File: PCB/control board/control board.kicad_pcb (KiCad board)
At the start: 2 copper layers, 27 parts, among them J1 JST-XH 1x05, J2 JST-XH 1x05, J3 JST-XH 1x05, SW1 SW_MEC_5E, SW2 SW_MEC_5E, SW3 SW_MEC_5E, SW4 SW_MEC_5E, SW5 SW_MEC_5E, SW6 SW_MEC_5E, SW7 SW_MEC_5E, SW8 SW_MEC_5E

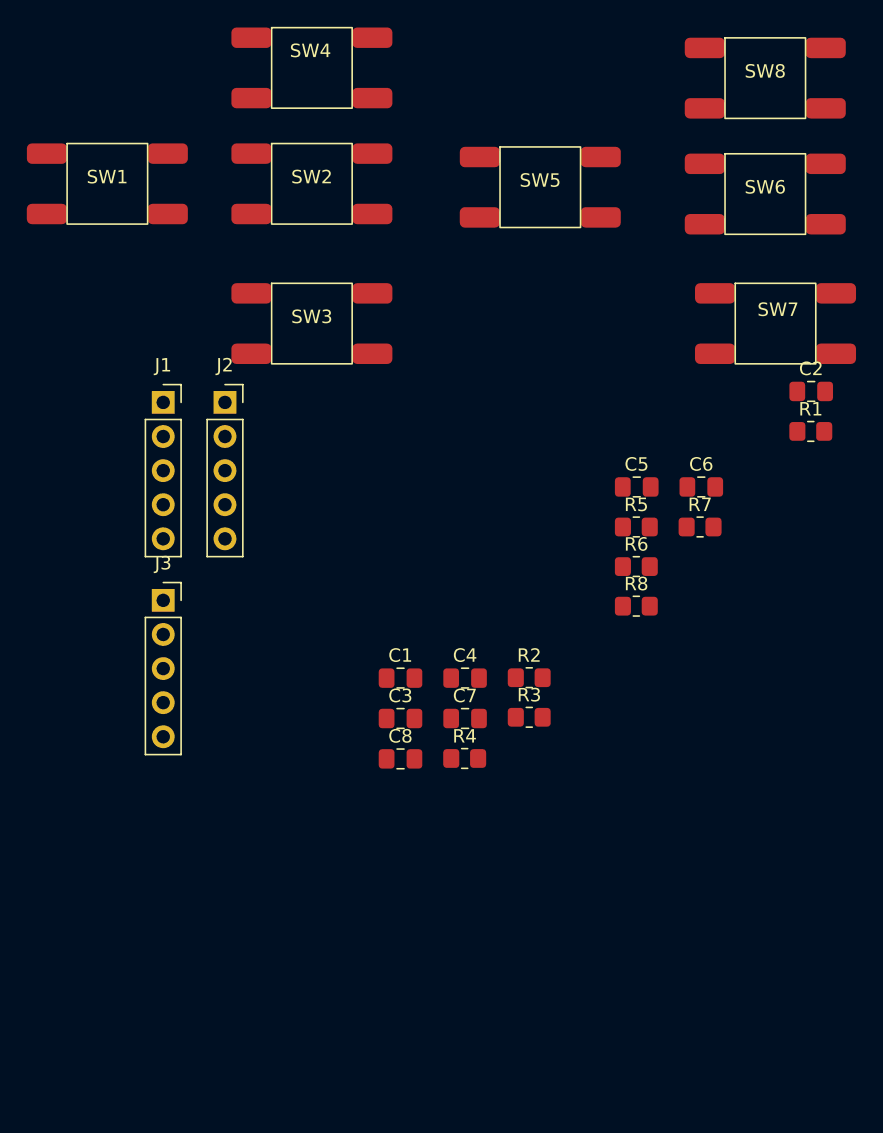
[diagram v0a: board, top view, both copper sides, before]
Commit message: Led board + control board
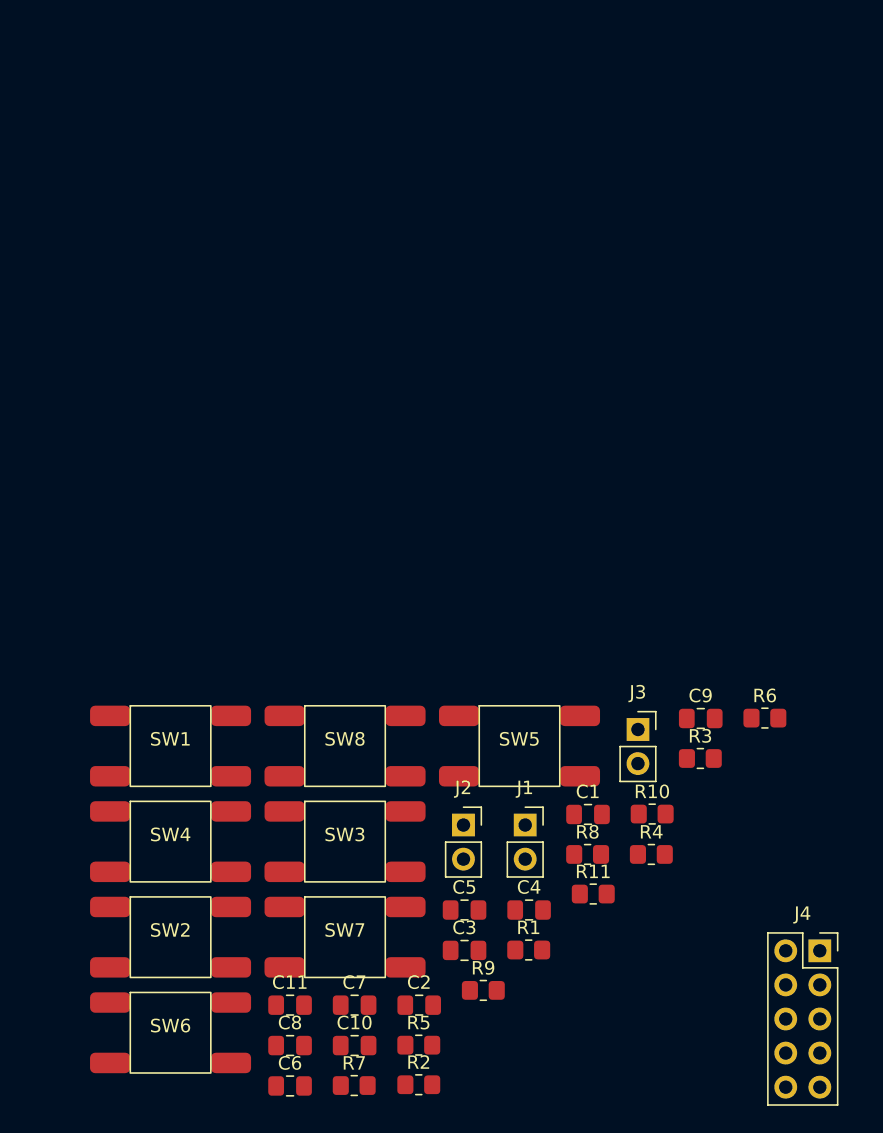
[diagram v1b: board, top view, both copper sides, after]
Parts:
- added C10: 100nF, Capacitor_SMD:C_0805_2012Metric_Pad1.18x1.45mm_HandSolder, F.Cu at (127.4, 125.9)
- added C11: 100nF, Capacitor_SMD:C_0805_2012Metric_Pad1.18x1.45mm_HandSolder, F.Cu at (122.6, 122.9)
- added C9: 100nF, Capacitor_SMD:C_0805_2012Metric_Pad1.18x1.45mm_HandSolder, F.Cu at (153.2, 101.6)
- added J4: Conn_02x05_Top_Bottom, Connector_PinSocket_2.54mm:PinSocket_2x05_P2.54mm_Vertical, F.Cu at (162.1, 118.9)
- added R10: 10k, Resistor_SMD:R_0805_2012Metric_Pad1.20x1.40mm_HandSolder, F.Cu at (149.6, 108.7)
- added R11: 10k, Resistor_SMD:R_0805_2012Metric_Pad1.20x1.40mm_HandSolder, F.Cu at (145.2, 114.6)
- added R9: 10k, Resistor_SMD:R_0805_2012Metric_Pad1.20x1.40mm_HandSolder, F.Cu at (137.0, 121.8)
- J1: value JST-XH 1x05 -> BTN1; footprint Connector_PinSocket_2.54mm:PinSocket_1x05_P2.54mm_Vertical -> Connector_PinSocket_2.54mm:PinSocket_1x02_P2.54mm_Vertical
- J2: value JST-XH 1x05 -> BTN2; footprint Connector_PinSocket_2.54mm:PinSocket_1x05_P2.54mm_Vertical -> Connector_PinSocket_2.54mm:PinSocket_1x02_P2.54mm_Vertical
- J3: value JST-XH 1x05 -> BTN3; footprint Connector_PinSocket_2.54mm:PinSocket_1x05_P2.54mm_Vertical -> Connector_PinSocket_2.54mm:PinSocket_1x02_P2.54mm_Vertical
- moved SW6 76.6 mm to (113.7, 125.0)
- moved SW8 58.8 mm to (126.7, 103.6)
- moved SW4 58.6 mm to (113.7, 110.7)
- moved SW2 57.1 mm to (113.7, 117.9)
- moved SW7 55.8 mm to (126.7, 117.9)
- moved C2 54.3 mm to (132.2, 122.9)
- moved C6 54.1 mm to (122.6, 128.9)
- moved R7 49.0 mm to (127.4, 128.9)
- moved R1 44.0 mm to (140.4, 118.8)
- moved SW1 42.2 mm to (113.7, 103.6)
- moved R5 41.9 mm to (132.2, 125.9)
- moved SW5 41.7 mm to (139.7, 103.6)
- moved J1 41.5 mm to (140.1, 109.5)
- moved SW3 38.7 mm to (126.7, 110.7)
- moved J3 36.7 mm to (148.5, 102.4)
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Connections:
- C2 pad 1: OK -> MENU
- C3 pad 1: DOWN -> OK
- C4 pad 1: UP -> DOWN
- C5 pad 1: RIGHT -> HOME
- C6 pad 1: BTN2 -> UP
- C7 pad 1: BTN3 -> RIGHT
- C8 pad 1: BTN1 -> BACK
- J1 pad 1: +3.3V -> GND
- J1 pad 2: UP -> BTN1
- J2 pad 1: OK -> GND
- J2 pad 2: BTN1 -> BTN2
- J3 pad 1: unconnected-(J3-Pad1) -> GND
- J3 pad 2: unconnected-(J3-Pad2) -> BTN3
- SW2 pad 3: OK -> MENU
- SW3 pad 3: DOWN -> OK
- SW4 pad 3: UP -> DOWN
- SW5 pad 3: RIGHT -> HOME
- SW6 pad 3: BTN2 -> UP
- SW7 pad 3: BTN3 -> RIGHT
- SW8 pad 3: BTN1 -> BACK

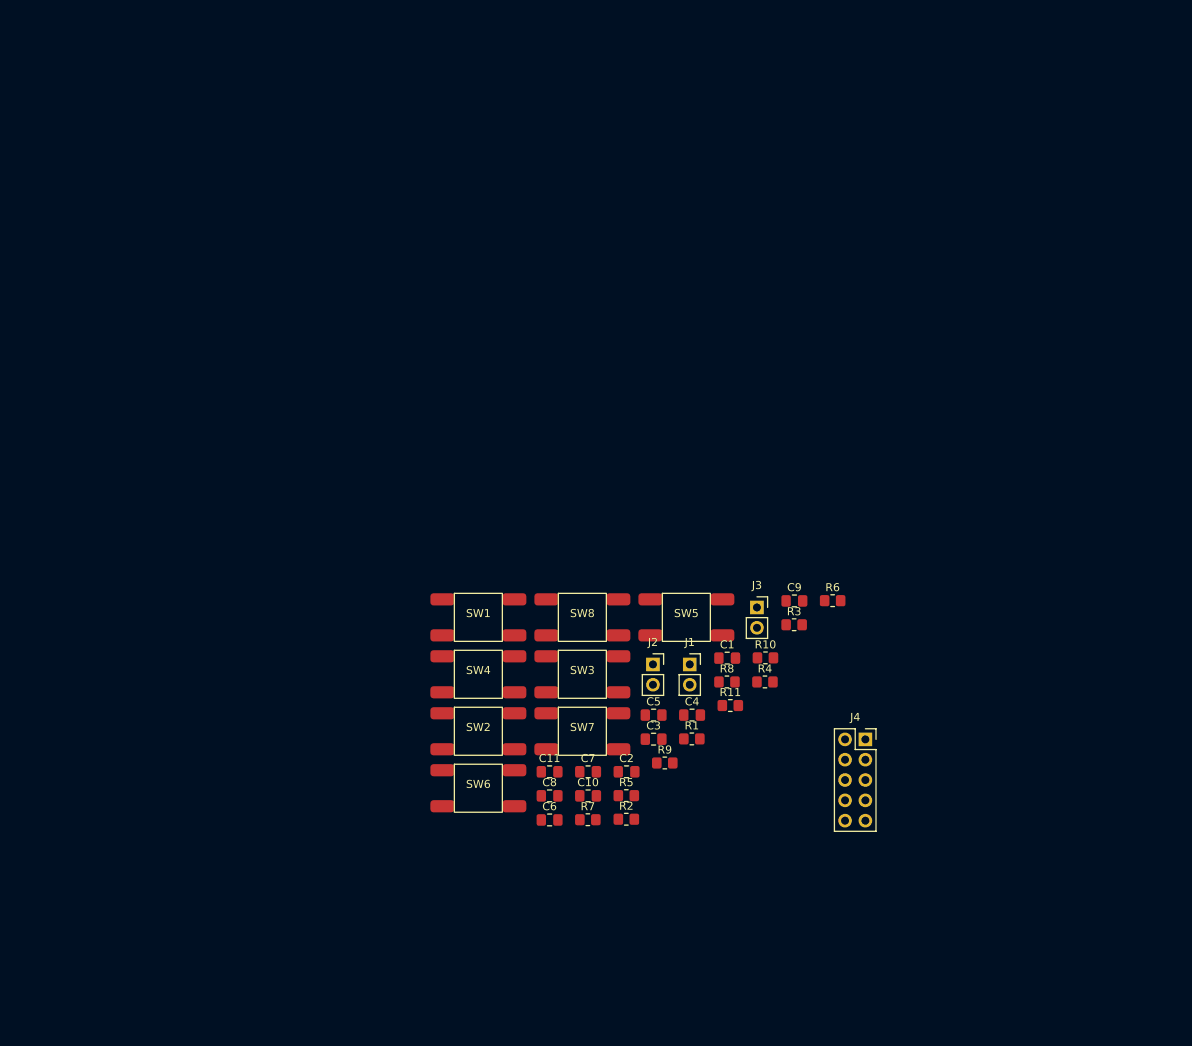
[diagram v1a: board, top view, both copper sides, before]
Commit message: control a led boarda hotový kromě popisku a děr
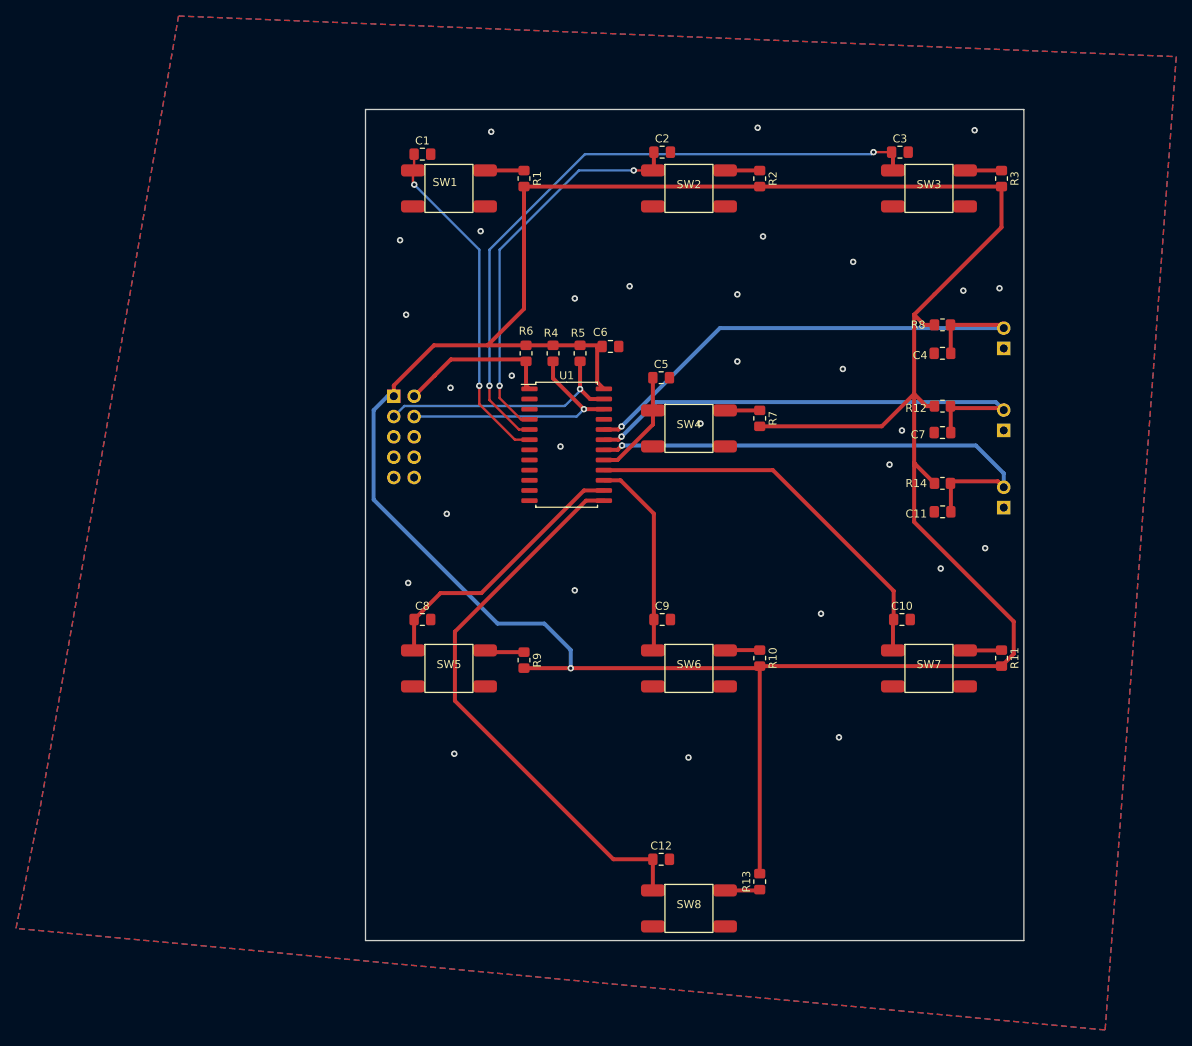
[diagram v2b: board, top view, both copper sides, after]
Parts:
- added C6: 100nF, Capacitor_SMD:C_0805_2012Metric_Pad1.18x1.45mm_HandSolder, F.Cu at (130.2, 69.8)
- added R4: 10k, Resistor_SMD:R_0805_2012Metric_Pad1.20x1.40mm_HandSolder, F.Cu at (123.0, 70.6)
- added R5: 10k, Resistor_SMD:R_0805_2012Metric_Pad1.20x1.40mm_HandSolder, F.Cu at (126.4, 70.6)
- added R6: 10k, Resistor_SMD:R_0805_2012Metric_Pad1.20x1.40mm_HandSolder, F.Cu at (119.6, 70.6)
- added U1: PCA9555D, Package_SO:SOIC-24W_7.5x15.4mm_P1.27mm, F.Cu at (124.7, 82.0)
- J1, J2: moved to B.Cu
- J3: renamed from J4; value Conn_02x05_Top_Bottom -> IDC_CONN; moved to B.Cu
- J4: renamed from J3; moved to B.Cu
- moved C3 91.6 mm to (166.4, 45.5)
- moved C1 81.3 mm to (106.7, 45.7)
- moved R1 81.1 mm to (119.4, 48.8), turned to -90 degrees
- moved R2 78.9 mm to (148.8, 48.8), turned to -90 degrees
- moved J3 72.9 mm to (103.1, 76.0), turned to 180 degrees
- moved R3 71.7 mm to (179.1, 48.8), turned to -90 degrees
- moved C2 70.4 mm to (136.7, 45.5)
- moved SW3 68.9 mm to (170.0, 50.0)
- moved SW1 68.0 mm to (110.0, 50.0)
- moved R8 64.8 mm to (171.7, 67.1), turned to 180 degrees
- moved C7 63.4 mm to (171.7, 80.5), turned to 180 degrees
- moved C11 58.9 mm to (171.7, 90.4), turned to 180 degrees
- moved C5 57.0 mm to (136.5, 73.7)
- moved J1 55.7 mm to (179.3, 70.0)
- moved R11 55.5 mm to (179.1, 108.7), turned to -90 degrees
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- renumbered C2 to C1, C7 to C10, C4 to C12, C5 to C2, C8 to C3, C9 to C4, C6 to C5, C10 to C7, C1 to C8, C3 to C9, R2 to R1, R3 to R10, R7 to R11, R10 to R12, R4 to R13, R11 to R14, R5 to R2, R8 to R3, R6 to R7, R9 to R8, R1 to R9, SW2 to SW1, SW5 to SW2, SW8 to SW3, SW6 to SW4, SW1 to SW5, SW3 to SW6, SW4 to SW8
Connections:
- J3 pad 1: unconnected-(J4-Pad1) -> +3.3V
- J3 pad 2: unconnected-(J4-Pad2) -> INT
- J3 pad 3: unconnected-(J4-Pad3) -> SDA
- J3 pad 4: unconnected-(J4-Pad4) -> SCL
- J3 pad 5: unconnected-(J4-Pad5) -> GND
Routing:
- net +3.3V: track 0.00 -> 353.0 mm, vias 0 -> 1
- net BACK: track 0.00 -> 83.0 mm, vias 0 -> 2
- net DOWN: track 0.00 -> 70.9 mm
- net BTN1: track 0.00 -> 65.6 mm, vias 0 -> 1
- net BTN3: track 0.00 -> 64.0 mm, vias 0 -> 1
- net BTN2: track 0.00 -> 62.5 mm, vias 0 -> 1
- net RIGHT: track 0.00 -> 50.0 mm
- net HOME: track 0.00 -> 48.8 mm, vias 0 -> 2
- net MENU: track 0.00 -> 42.8 mm, vias 0 -> 2
- net LEFT: track 0.00 -> 34.3 mm
- net SDA: track 0.00 -> 31.8 mm, vias 0 -> 1
- net SCL: track 0.00 -> 31.7 mm, vias 0 -> 1
- net OK: track 0.00 -> 25.1 mm
- net INT: track 0.00 -> 19.6 mm
- net UP: track 0.00 -> 13.8 mm
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- added copper zone on B.Cu, net GND
- added copper zone on F.Cu, net GND
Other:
- board outline added: 82.3 x 103.9 mm

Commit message: mount pro control,LED board.Komplet sensor board
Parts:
- added ?: , , F.Cu at (103.9, 139.7)
- added ?: , , F.Cu at (178.1, 139.7)
- added ?: , , F.Cu at (178.1, 43.9)
- added ?: , , F.Cu at (103.9, 43.9)
- moved C1 4.20 mm to (110.7, 46.8)
- moved C2 1.05 mm to (136.7, 46.5)
- moved C3 1.05 mm to (166.4, 46.5)
- moved R1 1.05 mm to (119.4, 49.8)
- moved R2 1.05 mm to (148.8, 49.8)
- moved R3 1.05 mm to (179.1, 49.8)
- moved SW1 1.05 mm to (110.0, 51.1)
- moved SW2 1.05 mm to (140.0, 51.1)
- moved SW3 1.05 mm to (170.0, 51.1)
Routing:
- net MENU: track 42.8 -> 45.4 mm
- net +3.3V: track 353.0 -> 350.9 mm
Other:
- board text added: "GORAK INDUSTRIES Project FENIX Control board V1.0"
